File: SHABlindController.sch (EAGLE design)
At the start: 48 parts, among them IC1 ATMEGA1284P-TQFP, IC2 XBEE-1B2, IC3 MOC3042S, IC4 MOC3042S, SW1 RESET, T1 MOC3042M, T2 MOC3042M, Y1 RESONATORSMD

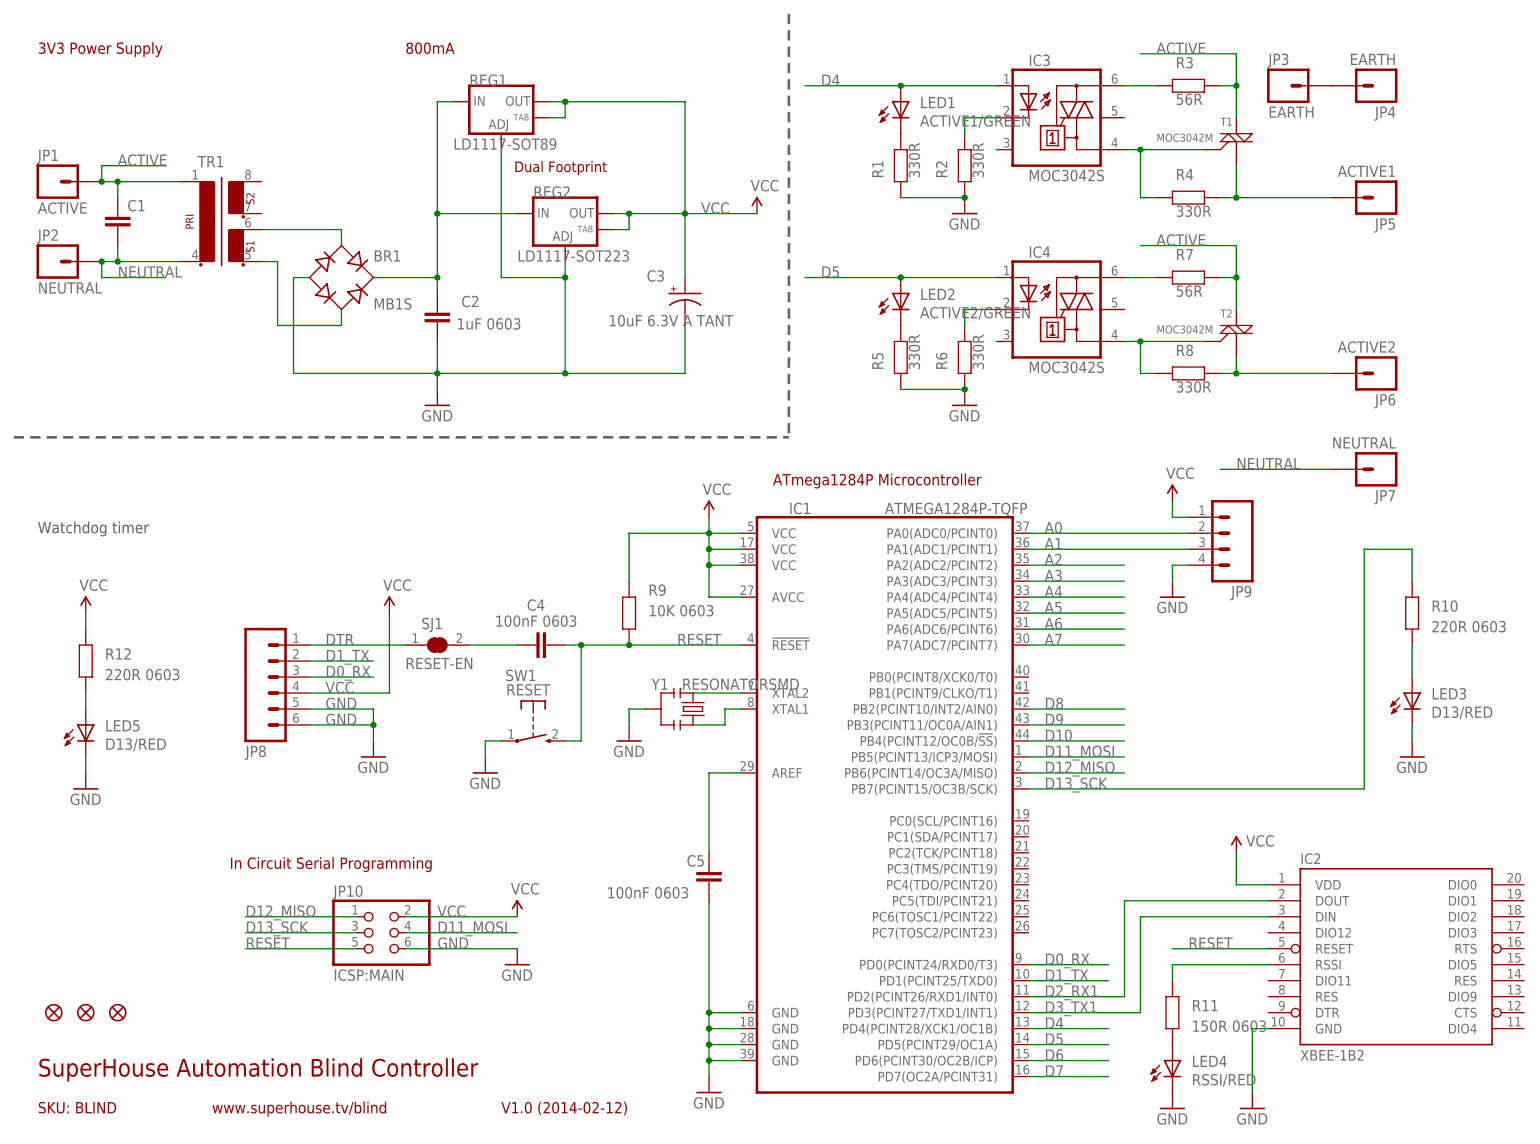
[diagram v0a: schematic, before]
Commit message: Replaced MCU and XBee with Spark Core
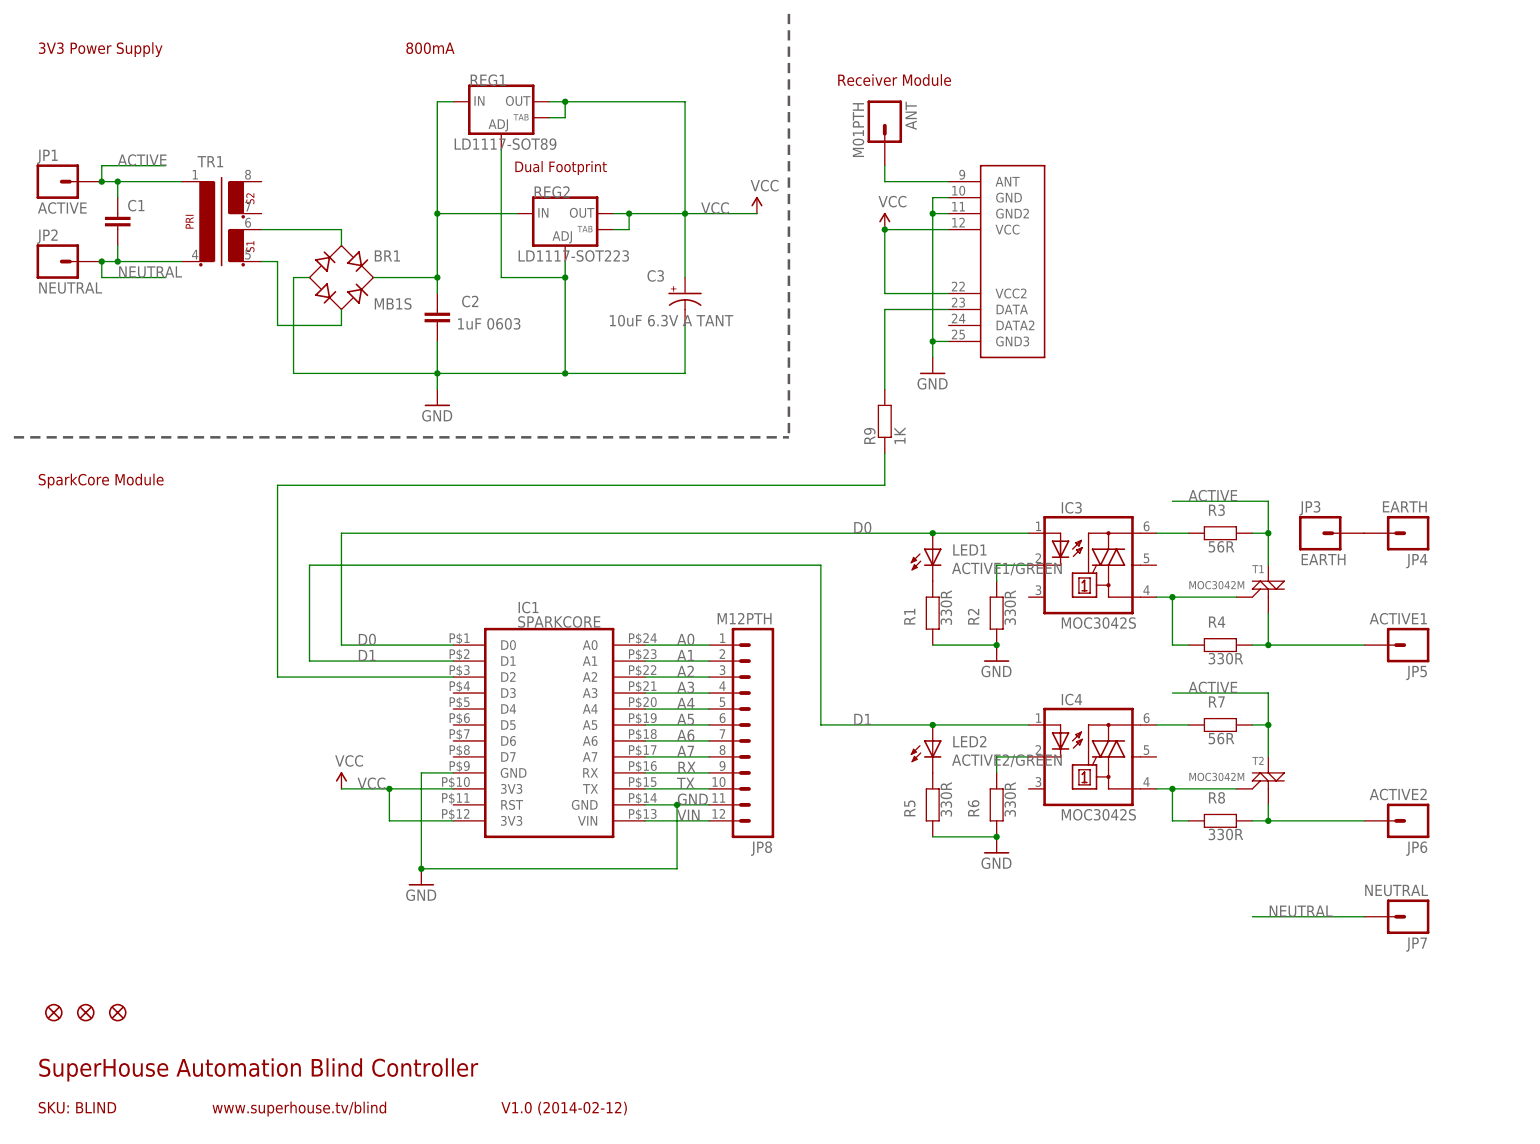
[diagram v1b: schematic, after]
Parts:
- removed C4, C5: 100nF 0603, freetronics:CAP0603
- removed IC2: XBEE-1B2, xbee:XBEE-1B2
- removed JP10: ICSP:MAIN, pinhead:PINHD-2X3
- removed JP9: (no value), freetronics-original:M04PTH
- removed LED3, LED5: D13/RED, freetronics:LED0603
- removed LED4: RSSI/RED, freetronics:LED0603
- removed R10, R12: 220R 0603, freetronics:RESISTOR0603
- removed R11: 150R 0603, freetronics:RESISTOR0603
- removed SJ1: RESET-EN, freetronics-jon:SJCN
- removed SW1: RESET, freetronics-master-v1:TAC_SWITCH_2PIN
- removed Y1: RESONATORSMD, SparkFun:RESONATORSMD
- added ANT: M01PTH, freetronics:M01PTH
- added RX1: RXB1SIL, PracticalArduino:RXB1SIL
- IC1: value ATMEGA1284P-TQFP -> SPARKCORE; device freetronics-jon:ATMEGA1284P-TQFP -> freetronics-jon:SPARKCORE
- JP8: value (none) -> M12PTH; device freetronics-master-v1.1:M06SIP -> freetronics-original:M12PTH
- R9: value 10K 0603 -> 1K
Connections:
- removed net D0_RX: IC1.PD0(PCINT24/RXD0/T3), JP8.3
- removed net D10: IC1.PB4(PCINT12/OC0B/!SS!)
- removed net D11_MOSI: IC1.PB5(PCINT13/ICP3/MOSI), JP10.4
- removed net D12_MISO: IC1.PB6(PCINT14/OC3A/MISO), JP10.1
- removed net D13_SCK: IC1.PB7(PCINT15/OC3B/SCK), JP10.3, R10.2
- removed net D1_TX: IC1.PD1(PCINT25/TXD0), JP8.2
- removed net D2_RX1: IC1.PD2(PCINT26/RXD1/INT0), IC2.DOUT
- removed net D3_TX1: IC1.PD3(PCINT27/TXD1/INT1), IC2.DIN
- removed net D4: IC1.PD4(PCINT28/XCK1/OC1B), IC3.1, LED1.A
- removed net D5: IC1.PD5(PCINT29/OC1A), IC4.1, LED2.A
- removed net D6: IC1.PD6(PCINT30/OC2B/ICP)
- removed net D7: IC1.PD7(OC2A/PCINT31)
- removed net D8: IC1.PB2(PCINT10/INT2/AIN0)
- removed net D9: IC1.PB3(PCINT11/OC0A/AIN1)
- removed net DTR: JP8.1, SJ1.1
- removed net N$11: C5.2, IC1.AREF
- removed net N$19: LED5.A, R12.1
- removed net N$23: IC2.RSSI, R11.2
- removed net N$24: LED4.A, R11.1
- removed net N$8: IC1.XTAL2, Y1.1
- removed net N$9: IC1.XTAL1, Y1.3
- removed net RESET: C4.2, IC1.!RESET, IC2.RESET, JP10.5, R9.1, SW1.S
- new net D0: IC1.D0, IC3.1, LED1.A
- new net D1: IC1.D1, IC4.1, LED2.A
- new net N$135: R9.2, RX1.DATA
- new net RX: IC1.RX, JP8.9
- new net TX: IC1.TX, JP8.10
- new net VIN: IC1.VIN, JP8.12
- net A0: now also IC1.A0, JP8.1; no longer IC1.PA0(ADC0/PCINT0), JP9.2
- net A1: now also IC1.A1, JP8.2; no longer IC1.PA1(ADC1/PCINT1), JP9.3
- net A2: now also IC1.A2, JP8.3; no longer IC1.PA2(ADC2/PCINT2)
- net A3: now also IC1.A3, JP8.4; no longer IC1.PA3(ADC3/PCINT3)
- net A4: now also IC1.A4, JP8.5; no longer IC1.PA4(ADC4/PCINT4)
- net A5: now also IC1.A5, JP8.6; no longer IC1.PA5(ADC5/PCINT5)
- net A6: now also IC1.A6, JP8.7; no longer IC1.PA6(ADC6/PCINT6)
- net A7: now also IC1.A7, JP8.8; no longer IC1.PA7(ADC7/PCINT7)
- net GND: now also JP8.11, RX1.GND, RX1.GND2, RX1.GND3; no longer C5.1, IC1.GND@3, IC1.GND@4, IC2.GND, JP10.6, JP8.5, JP8.6, JP9.4, LED3.C, LED4.C, LED5.C, SW1.P, Y1.2
- net N$1: now also ANT.1, RX1.ANT; no longer LED3.A, R10.1
- net N$3: now also IC1.D2, R9.1; no longer C4.1, SJ1.2
- net VCC: now also IC1.3V3@1, IC1.3V3@2, RX1.VCC, RX1.VCC2; no longer IC1.AVCC, IC1.VCC@1, IC1.VCC@2, IC1.VCC@3, IC2.VDD, JP10.2, JP8.4, JP9.1, R12.2, R9.2
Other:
- note added: "Receiver Module"
- note added: "SparkCore Module"
- note removed: "ATmega1284P Microcontroller"
- note removed: "In Circuit Serial Programming"
- note removed: "Watchdog timer"
- moved on the sheet: IC3, IC4, JP3, JP4, JP5, JP6, JP7, LED1, LED2, R1, R2, R3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

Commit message: Improved routing for v2.0 release
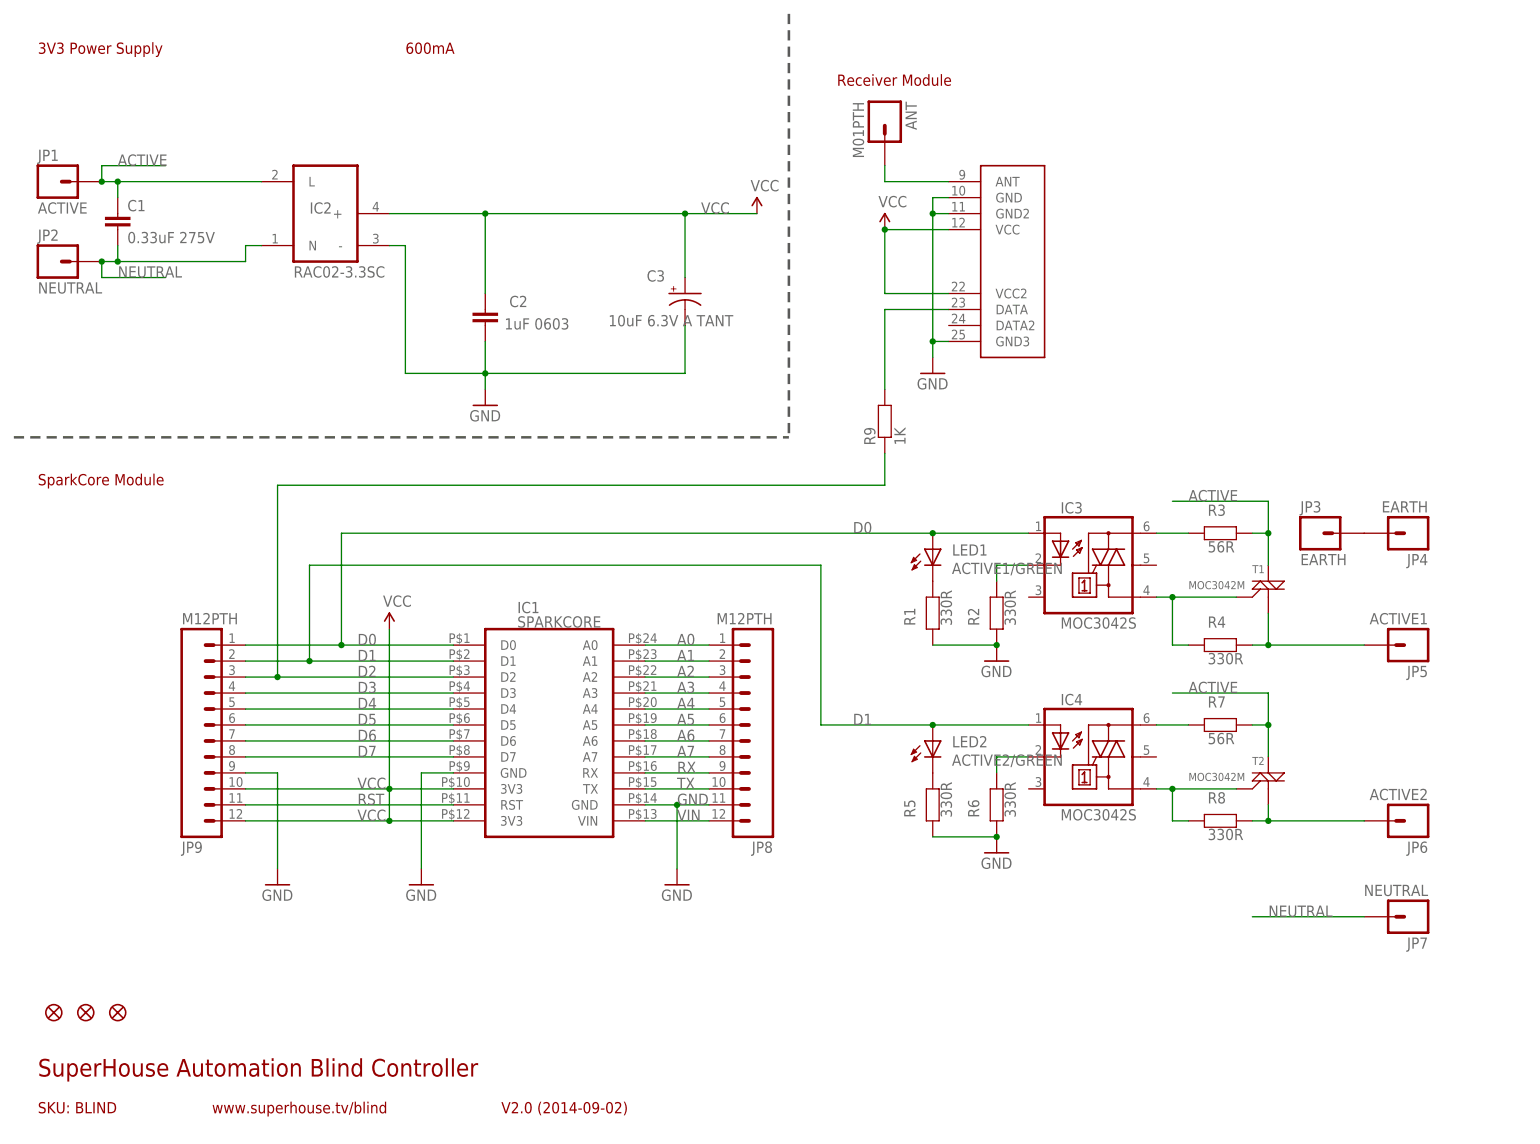
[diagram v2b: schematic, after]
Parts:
- removed BR1: MB1S, rectifier:MB1S
- removed REG1: LD1117-SOT89, freetronics:V_REG_LM1117SOT89
- removed REG2: LD1117-SOT223, freetronics:V_REG_LM1117SOT223
- removed TR1: (no value), freetronics-jon:EE20-2
- added IC2: RAC02-3.3SC, freetronics-jon:RAC0X-SC
- added JP9: M12PTH, freetronics-original:M12PTH
- C1: value (none) -> 0.33uF 275V
- renumbered RX1 to IC5
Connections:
- removed net N$3: IC1.D2, R9.1
- removed net N$5: BR1.+, C2.1, REG1.IN, REG2.IN
- removed net N$6: BR1.AC1, TR1.4
- removed net N$7: BR1.AC2, TR1.3
- new net D2: IC1.D2, JP9.3, R9.1
- new net D3: IC1.D3, JP9.4
- new net D4: IC1.D4, JP9.5
- new net D5: IC1.D5, JP9.6
- new net D6: IC1.D6, JP9.7
- new net D7: IC1.D7, JP9.8
- new net RST: IC1.RST, JP9.11
- net ACTIVE: now also IC2.L; no longer TR1.1
- net D0: now also JP9.1
- net D1: now also JP9.2
- net GND: now also IC2.-, JP9.9; no longer BR1.-, REG1.ADJ, REG2.ADJ
- net NEUTRAL: now also IC2.N; no longer TR1.2
- net VCC: now also C2.1, IC2.+, JP9.10, JP9.12; no longer REG1.OUT, REG1.OUT@1, REG2.OUT, REG2.OUT@1
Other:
- note added: "600mA"
- note added: "V2.0 (2014-09-02)"
- note removed: "800mA"
- note removed: "Dual Footprint"
- note removed: "V1.0 (2014-02-12)"
- moved on the sheet: C2
